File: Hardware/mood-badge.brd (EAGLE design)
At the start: 76.2 x 101.6 mm, 0 parts

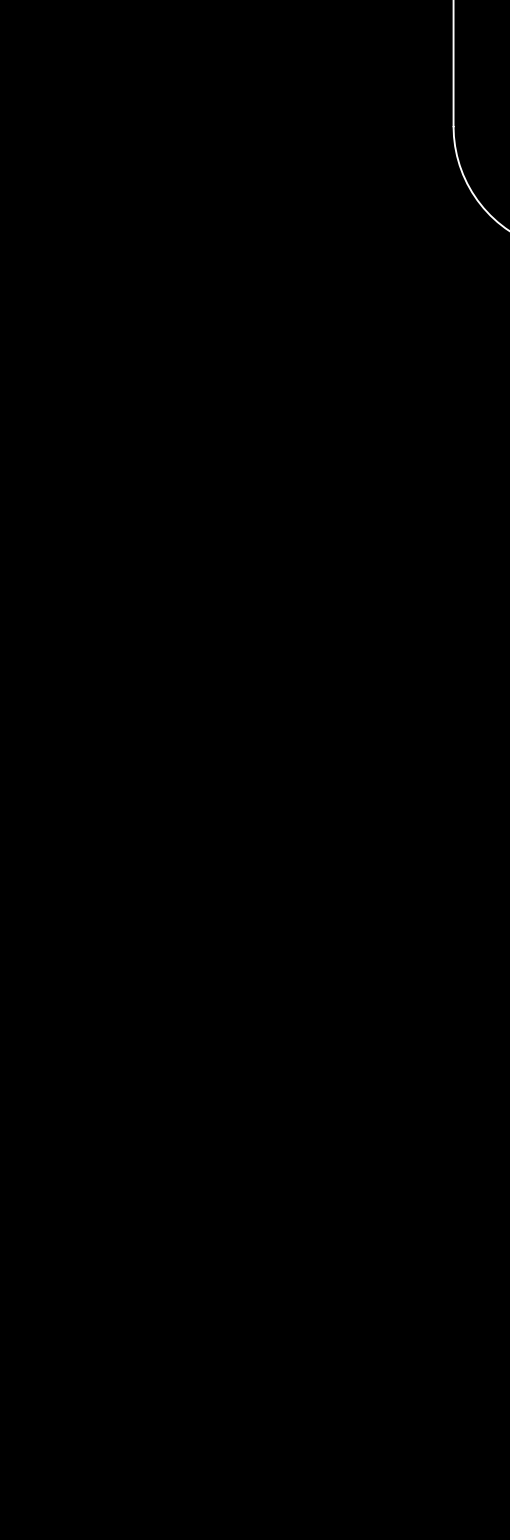
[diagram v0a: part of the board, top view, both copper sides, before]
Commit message: Added microcontroller unit and started on power supply design
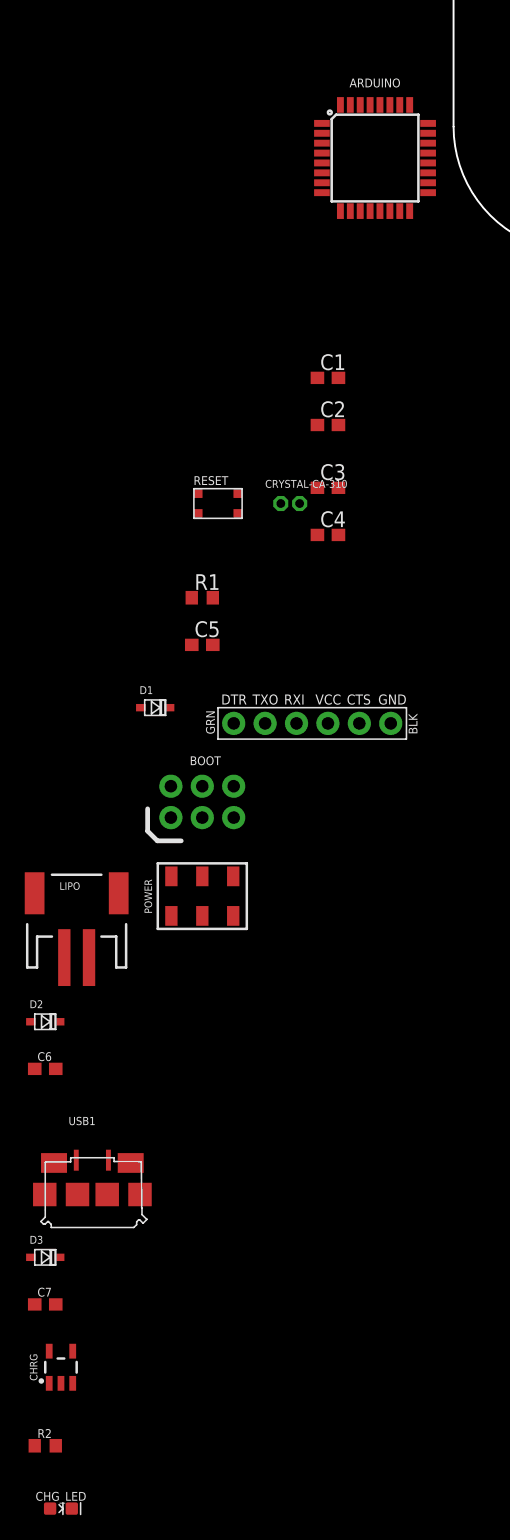
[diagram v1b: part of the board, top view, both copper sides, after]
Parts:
- added ARDUINO: ATMEGA328P_TQFP, LinnesLab-Microcontrollers:TQFP32-08
- added BOOT: AVR_SPI_PROG_3X2NS, LinnesLab-Connectors:2X3-NS
- added C1, C2: 22p, LinnesLab-Passives:C0603
- added C3, C5: 0.1u, LinnesLab-Passives:C0603
- added C4: 2.2u, LinnesLab-Passives:C0603
- added C6, C7: 4.7u, LinnesLab-Passives:C0603
- added CHG_LED: (no value), LinnesLab-LED:LED-0603
- added CHRG: MCP73831.SOT23-5, LinnesLab-Power:SOT23-5
- added CRYSTAL-CA-310: (no value), LinnesLab-Clocks:CA-301
- added D1, D2, D3: (no value), LinnesLab-DiscreteSemi:USC
- added FTDI: FTDI_DEVICE, LinnesLab-Connectors:FTDI_DEVICE
- added LIPO: (no value), LinnesLab-Connectors:JST-2-SMD
- added POWER: SWITCH.JS202011JXQNUPWARDS, LinnesLab-Switches:SWITCH.00
- added R1: 10k, LinnesLab-Passives:R0603
- added R2: 1k, LinnesLab-Passives:R0603
- added RESET: (no value), LinnesLab-Switches:BUTTON-GULLWING
- added USB1: USB.MICRO.PWR-BIGGERPADS, LinnesLab-Connectors:USB-MICRO-01.BIGGERPADS.PWR
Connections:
- new net ACTION: ARDUINO.19
- new net DTR: C5.1, FTDI.DTR
- new net GND: ARDUINO.21, ARDUINO.3, ARDUINO.5, BOOT.6, C1.2, C2.2, C3.2, C4.2, C6.2, C7.2, FTDI.CTS, FTDI.GND, LIPO.1, RESET.1, RESET.2, USB1.5
- new net LD1: ARDUINO.2
- new net LD10: ARDUINO.16, BOOT.1
- new net LD11: ARDUINO.15, BOOT.4
- new net LD12: ARDUINO.14
- new net LD13: ARDUINO.13
- new net LD14: ARDUINO.12
- new net LD15: ARDUINO.11
- new net LD16: ARDUINO.10
- new net LD2: ARDUINO.1
- new net LD3: ARDUINO.32
- new net LD4: ARDUINO.28
- new net LD5: ARDUINO.27
- new net LD6: ARDUINO.26
- new net LD7: ARDUINO.25
- new net LD8: ARDUINO.24
- new net LD9: ARDUINO.17, BOOT.3
- new net LEFT: ARDUINO.23
- new net MODE: ARDUINO.9
- new net N$1: ARDUINO.7, C1.1, CRYSTAL-CA-310.1
- new net N$2: ARDUINO.8, C2.1, CRYSTAL-CA-310.2
- new net N$3: CHG_LED.A, R2.1
- new net N$4: D3.+, USB1.1
- new net N$5: D2.+, POWER.1
- new net N$6: D1.+, FTDI.VCC
- new net RESET: ARDUINO.29, BOOT.5, C5.2, R1.1, RESET.3, RESET.4
- new net RIGHT: ARDUINO.22
- new net RXD: ARDUINO.30, FTDI.TXO
- new net STAT: CHG_LED.C, CHRG.1
- new net TXD: ARDUINO.31, FTDI.RXI
- new net VBAT: CHRG.3
- new net VCC: ARDUINO.18, ARDUINO.4, ARDUINO.6, BOOT.2, C3.1, C4.1, C6.1, C7.1, CHRG.4, D1.-, D2.-, D3.-, R1.2, R2.2
- new net VLIPO: LIPO.2, POWER.2
- new net VSS: CHRG.2

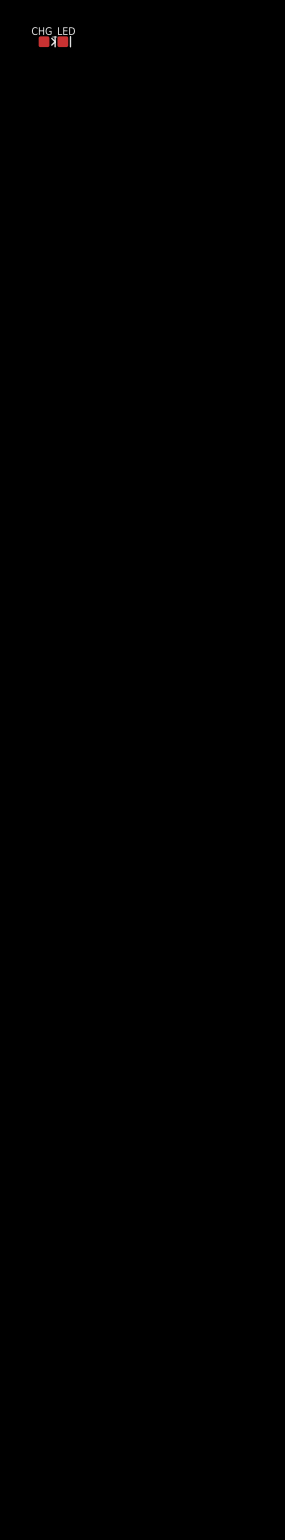
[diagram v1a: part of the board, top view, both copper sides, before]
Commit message: Finished charger circuit and added action buttons
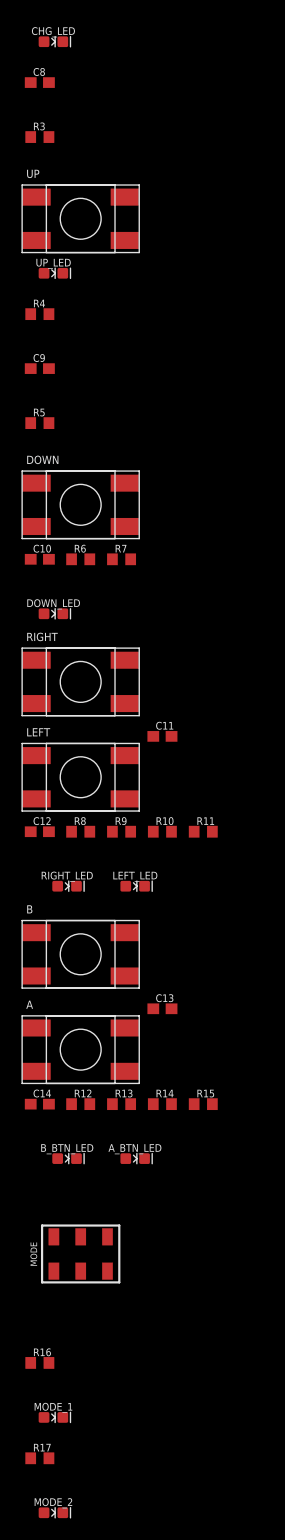
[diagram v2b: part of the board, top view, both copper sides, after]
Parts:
- added A, B, DOWN, LEFT, RIGHT, UP: (no value), LinnesLab-Switches:SPST.KT11P4SM34LFS
- added A_BTN_LED, B_BTN_LED, DOWN_LED, LEFT_LED, MODE_1, MODE_2, RIGHT_LED, UP_LED: (no value), LinnesLab-LED:LED-0603
- added C10, C11, C12, C13, C14, C9: 100n, LinnesLab-Passives:C0603
- added C8: 4.7u, LinnesLab-Passives:C0603
- added MODE: SWITCH.JS202011JXQNUPWARDS, LinnesLab-Switches:SWITCH.00
- added R10, R12, R14, R3, R4, R6, R8: 10k, LinnesLab-Passives:R0603
- added R11, R13, R15, R16, R17, R5, R7, R9: 1k, LinnesLab-Passives:R0603
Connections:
- removed net VBAT: CHRG.3
- removed net VSS: CHRG.2
- new net N$10: C10.1, DOWN.3, DOWN.4, DOWN_LED.A, R6.1
- new net N$11: DOWN_LED.C, R7.1
- new net N$12: C11.1, LEFT.3, LEFT.4, LEFT_LED.A, R8.1
- new net N$13: LEFT_LED.C, R9.1
- new net N$14: C12.1, R10.1, RIGHT.3, RIGHT.4, RIGHT_LED.A
- new net N$15: R11.1, RIGHT_LED.C
- new net N$16: A.3, A.4, A_BTN_LED.A, C13.1, R12.1
- new net N$17: A_BTN_LED.C, R13.1
- new net N$18: B.3, B.4, B_BTN_LED.A, C14.1, R14.1
- new net N$19: B_BTN_LED.C, R15.1
- new net N$21: MODE_2.C, R17.1
- new net N$22: MODE_1.C, R16.1
- new net N$7: CHRG.5, R3.1
- new net N$8: C9.1, R4.1, UP.3, UP.4, UP_LED.A
- new net N$9: R5.1, UP_LED.C
- net GND: now also C10.2, C11.2, C12.2, C13.2, C14.2, C8.2, C9.2, CHRG.2, MODE.1, R10.2, R11.2, R12.2, R13.2, R14.2, R15.2, R16.2, R3.2, R4.2, R5.2, R6.2, R7.2, R8.2, R9.2
- net MODE: now also MODE.2, MODE_1.A, R17.2
- net VCC: now also A.1, A.2, B.1, B.2, DOWN.1, DOWN.2, LEFT.1, LEFT.2, MODE.3, MODE_2.A, RIGHT.1, RIGHT.2, UP.1, UP.2
- net VLIPO: now also C8.1, CHRG.3

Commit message: Pulse sensor and LiPo voltage booster to use 5v logic
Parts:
- removed C6: 4.7u, LinnesLab-Passives:C0603
- added C15, C16, C18: 4.7u, LinnesLab-Passives:C0603
- added C17: 2.2u, LinnesLab-Passives:C0603
- added C19, C21: 100n, LinnesLab-Passives:C0603
- added C20: 1u, LinnesLab-Passives:C0603
- added C22, C23, C24: 22u, LinnesLab-Passives:C0603
- added D4, D5: (no value), LinnesLab-DiscreteSemi:USC
- added L1: 2.2u, LinnesLab-Passives:L0603
- added LED1: (no value), LinnesLab-LED:LED_5MM
- added LED2: (no value), LinnesLab-LED:LED-0603
- added OP1: (no value), LinnesLab-AnalogIC:SOT23-5
- added R18: 10k, LinnesLab-Passives:R0603
- added R19: 3.3M, LinnesLab-Passives:R0603
- added R20: 12K, LinnesLab-Passives:R0603
- added R21, R22: 210K, LinnesLab-Passives:R0603
- added R23: 487, LinnesLab-Passives:R0603
- added R24, R27: 750K, LinnesLab-Passives:R0603
- added R25: 100k, LinnesLab-Passives:R0603
- added R26: 100K, LinnesLab-Passives:R0603
- added R28: 4.7K, LinnesLab-Passives:R0603
- added U$1: ADPS9008, LinnesLab-Sensors:6-PIN.CHIPLED
- added U$2: PCF8575C, SparkFun-Retired:SO-24DW
- added U1: PAM2401, SparkFun-IC-Power:MSOP8
- R2: value 1k -> 100k
- USB1: value USB.MICRO.PWR-BIGGERPADS -> USB.MICRO-BIGGERPADS; device LinnesLab-Connectors:USB-MICRO-01.BIGGERPADS.PWR -> LinnesLab-Connectors:USB-MICRO-01.BIGGERPADS
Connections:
- net LD10 renamed MISO
- net LD11 renamed MOSI
- net LD9 renamed SCK
- net N$4 renamed V_USB
- removed net LD4: ARDUINO.28
- removed net LD5: ARDUINO.27
- new net ENABLE: R24.1, U1.2
- new net N$20: C15.1, R20.1, U$1.6
- new net N$23: C15.2, C16.1, C18.1
- new net N$24: C16.2, C17.1, R18.1
- new net N$25: C17.2, OP1.3, R21.2, R22.1
- new net N$26: OP1.4, R18.2, R19.1
- new net N$27: R25.1, U1.6
- new net N$28: LED1.K, R23.1
- new net N$29: L1.2, U1.1
- new net N$30: R26.2, R27.1, U1.5
- new net N$32: LED2.C, R28.2
- new net PULSE: OP1.1, R19.2
- new net SCL: ARDUINO.28, U$2.22
- new net SDA: ARDUINO.27, U$2.23
- net GND: now also C18.2, C19.1, C20.2, C21.2, C22.2, C23.2, C24.2, D4.+, D5.+, OP1.2, R20.2, R22.2, R23.2, R25.2, R26.1, R28.1, U$1.4, U$2.12, U$2.2, U$2.21, U$2.3, U1.4, U1.8; no longer C6.2
- net VCC: now also C19.2, C20.1, C21.1, C23.1, C24.1, D4.-, D5.-, LED1.A, LED2.A, OP1.5, R21.1, R27.2, U$1.1, U$2.24, U1.7; no longer C6.1, D2.-
- net VLIPO: now also C22.1, D2.-, L1.1, R24.2, U1.3

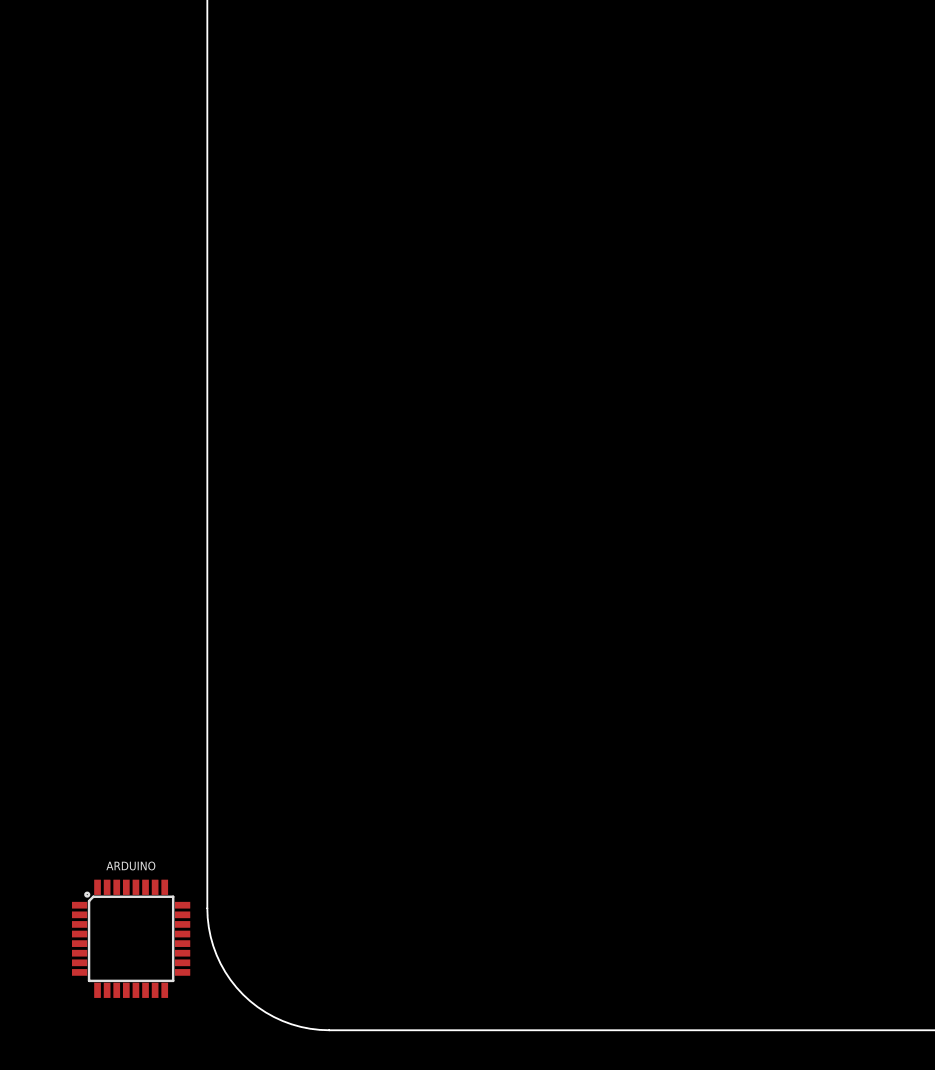
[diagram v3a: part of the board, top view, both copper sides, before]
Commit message: Adafruit 8x8 Dotstar Matrix Part
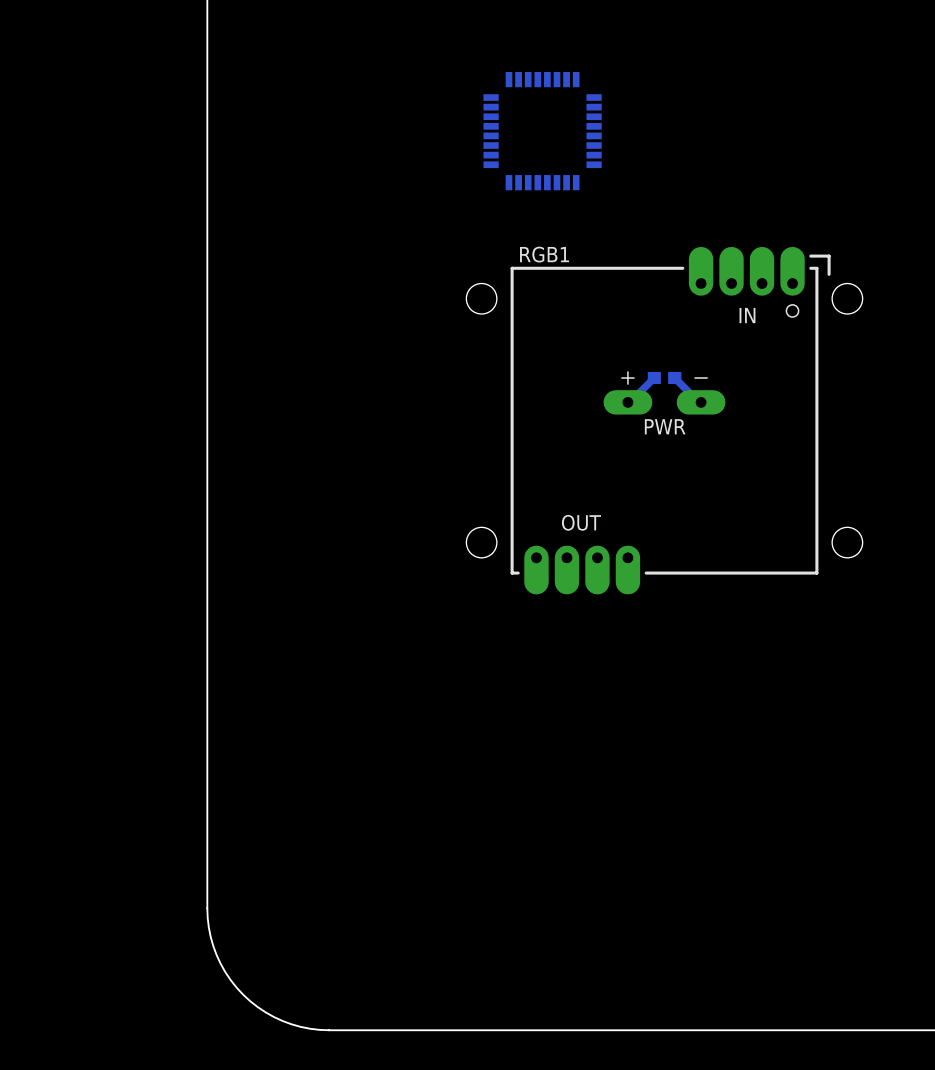
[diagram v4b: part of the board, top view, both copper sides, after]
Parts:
- added C6: 220u, LinnesLab-Passives:C0603
- added RGB1: (no value), mood-badge-components:ADA_DOTSTAR_8X8_3444_HOLES
- moved ARDUINO 75.5 mm to (27.9, 74.9), flipped to the bottom
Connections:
- net GND: now also C6.2, RGB1.GND, RGB1.GND_IN, RGB1.GND_OUT
- net MOSI: now also RGB1.DIN
- net SCK: now also RGB1.CIN
- net VCC: now also C6.1, RGB1.VDD, RGB1.VDD_IN, RGB1.VDD_OUT
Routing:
- net VCC: track 0.00 -> 2.52 mm
- net GND: track 0.00 -> 2.52 mm

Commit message: PCB layout work
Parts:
- removed CRYSTAL-CA-310: (no value), LinnesLab-Clocks:CA-301
- removed LED2: (no value), LinnesLab-LED:LED-0603
- removed U$1: ADPS9008, LinnesLab-Sensors:6-PIN.CHIPLED
- removed U$2: PCF8575C, SparkFun-Retired:SO-24DW
- removed U1: PAM2401, SparkFun-IC-Power:MSOP8
- added BOOST: PAM2401, SparkFun-IC-Power:MSOP8
- added I/O: PCF8575C, SparkFun-Retired:SO-24DW
- added PWR_LED: (no value), LinnesLab-LED:LED-0603
- added SENS1: ADPS9008, LinnesLab-Sensors:6-PIN.CHIPLED
- added XTAL: (no value), LinnesLab-Clocks:CA-301
- C6: device LinnesLab-Passives:C0603 -> LinnesLab-Passives:C1206
- LED1: device LinnesLab-LED:LED_5MM -> LinnesLab-LED:LED-0603
- moved R28 454.8 mm to (14.7, 87.9)
- moved C21 434.2 mm to (33.0, 113.8), flipped to the bottom, turned to 270 degrees
- moved C19 424.3 mm to (72.4, 111.5), flipped to the bottom
- moved D5 423.8 mm to (10.9, 48.3), flipped to the bottom, turned to 90 degrees
- moved C20 423.8 mm to (30.5, 108.7), flipped to the bottom, turned to 180 degrees
- moved C18 423.6 mm to (82.5, 123.2), flipped to the bottom
- moved R21 421.4 mm to (80.0, 116.6), flipped to the bottom
- moved R18 421.4 mm to (80.0, 143.3), flipped to the bottom
- moved R19 421.4 mm to (80.0, 131.8), flipped to the bottom
- moved R20 421.4 mm to (80.0, 126.7), flipped to the bottom
- moved R22 421.4 mm to (80.0, 111.5), flipped to the bottom
- moved D4 420.4 mm to (13.2, 48.3), flipped to the bottom, turned to 90 degrees
- moved C24 407.2 mm to (16.3, 48.5), flipped to the bottom, turned to 180 degrees
- moved C23 400.2 mm to (16.3, 46.5), flipped to the bottom, turned to 180 degrees
- moved R23 396.7 mm to (27.2, 86.9), turned to 270 degrees
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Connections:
- new net VIN: BOOST.3, C22.1, C7.1, CHRG.4, D2.-, D3.-, L1.1, R2.2, R24.2
- net ENABLE: now also BOOST.2; no longer U1.2
- net GND: now also BOOST.4, BOOST.8, I/O.12, I/O.2, I/O.21, I/O.3, SENS1.4; no longer U$1.4, U$2.12, U$2.2, U$2.21, U$2.3, U1.4, U1.8
- net N$1: now also XTAL.1; no longer CRYSTAL-CA-310.1
- net N$2: now also XTAL.2; no longer CRYSTAL-CA-310.2
- net N$20: now also SENS1.6; no longer U$1.6
- net N$27: now also BOOST.6; no longer U1.6
- net N$28: now also LED1.C; no longer LED1.K
- net N$29: now also BOOST.1; no longer U1.1
- net N$30: now also BOOST.5; no longer U1.5
- net N$32: now also PWR_LED.C; no longer LED2.C
- net SCL: now also I/O.22; no longer U$2.22
- net SDA: now also I/O.23; no longer U$2.23
- net VCC: now also BOOST.7, I/O.24, PWR_LED.A, SENS1.1; no longer C7.1, CHRG.4, D3.-, LED2.A, R2.2, U$1.1, U$2.24, U1.7
- net VLIPO: no longer C22.1, D2.-, L1.1, R24.2, U1.3
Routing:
- net VIN: track 0.00 -> 47.2 mm, vias 0 -> 1
- net VLIPO: track 0.00 -> 42.2 mm
- net GND: track 2.52 -> 41.6 mm, vias 0 -> 6
- net VCC: track 2.52 -> 18.5 mm, vias 0 -> 1
- net N$10: track 0.00 -> 10.8 mm
- net N$30: track 0.00 -> 8.63 mm
- net N$12: track 0.00 -> 8.34 mm
- net N$8: track 0.00 -> 7.92 mm
- net N$14: track 0.00 -> 7.51 mm
- net N$16: track 0.00 -> 7.32 mm
- net N$18: track 0.00 -> 7.32 mm
- net STAT: track 0.00 -> 6.30 mm, vias 0 -> 1
- net N$27: track 0.00 -> 5.06 mm
- net N$29: track 0.00 -> 3.35 mm
- net N$13: track 0.00 -> 2.84 mm
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- added copper zone on layer 16, net GND
- added copper zone on layer 1, net VCC
